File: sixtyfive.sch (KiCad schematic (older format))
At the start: 20 parts

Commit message: diagrammed mcu
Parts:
- added D? (x66): D_Small, symbol Device:D_Small
- added J?: Conn_ARM_JTAG_SWD_10, symbol Connector:Conn_ARM_JTAG_SWD_10
- added MX?: 6, symbol MX_Alps_Hybrid:MX-NoLED
- added MX?: 7, symbol MX_Alps_Hybrid:MX-NoLED
- added MX?: Y, symbol MX_Alps_Hybrid:MX-NoLED
- added MX?: U, symbol MX_Alps_Hybrid:MX-NoLED
- added MX?: 8, symbol MX_Alps_Hybrid:MX-NoLED
- added MX?: 9, symbol MX_Alps_Hybrid:MX-NoLED
- added MX?: I, symbol MX_Alps_Hybrid:MX-NoLED
- added MX?: O, symbol MX_Alps_Hybrid:MX-NoLED
- added MX?: 0, symbol MX_Alps_Hybrid:MX-NoLED
- added MX?: -, symbol MX_Alps_Hybrid:MX-NoLED
- added MX?: P, symbol MX_Alps_Hybrid:MX-NoLED
- added MX?: [{, symbol MX_Alps_Hybrid:MX-NoLED
- added MX?: =, symbol MX_Alps_Hybrid:MX-NoLED
- added MX?: Backspace, symbol MX_Alps_Hybrid:MX-NoLED
- added MX?: ]}, symbol MX_Alps_Hybrid:MX-NoLED
- added MX?: \\|, symbol MX_Alps_Hybrid:MX-NoLED
- added MX?: H, symbol MX_Alps_Hybrid:MX-NoLED
- added MX?: J, symbol MX_Alps_Hybrid:MX-NoLED
- added MX?: N, symbol MX_Alps_Hybrid:MX-NoLED
- added MX?: M, symbol MX_Alps_Hybrid:MX-NoLED
- added MX?: K, symbol MX_Alps_Hybrid:MX-NoLED
- added MX?: L, symbol MX_Alps_Hybrid:MX-NoLED
- added MX?: ,<, symbol MX_Alps_Hybrid:MX-NoLED
- added MX?: .>, symbol MX_Alps_Hybrid:MX-NoLED
- added MX?: :;, symbol MX_Alps_Hybrid:MX-NoLED
- added MX?: \"', symbol MX_Alps_Hybrid:MX-NoLED
- added MX?: ?/, symbol MX_Alps_Hybrid:MX-NoLED
- added MX?: RightShift, symbol MX_Alps_Hybrid:MX-NoLED
- added MX?: Enter, symbol MX_Alps_Hybrid:MX-NoLED
- added MX?: PgUp, symbol MX_Alps_Hybrid:MX-NoLED
- added MX?: Up, symbol MX_Alps_Hybrid:MX-NoLED
- added MX? (x2): MX-NoLED, symbol MX_Alps_Hybrid:MX-NoLED
- added MX?: 2, symbol MX_Alps_Hybrid:MX-NoLED
- added MX?: 3, symbol MX_Alps_Hybrid:MX-NoLED
- added MX?: W, symbol MX_Alps_Hybrid:MX-NoLED
- added MX?: E, symbol MX_Alps_Hybrid:MX-NoLED
- added MX?: 4, symbol MX_Alps_Hybrid:MX-NoLED
- added MX?: 5, symbol MX_Alps_Hybrid:MX-NoLED
- added MX?: R, symbol MX_Alps_Hybrid:MX-NoLED
- added MX?: T, symbol MX_Alps_Hybrid:MX-NoLED
- added MX?: S, symbol MX_Alps_Hybrid:MX-NoLED
- added MX?: D, symbol MX_Alps_Hybrid:MX-NoLED
- added MX?: X, symbol MX_Alps_Hybrid:MX-NoLED
- added MX?: C, symbol MX_Alps_Hybrid:MX-NoLED
- added MX?: F, symbol MX_Alps_Hybrid:MX-NoLED
- added MX?: G, symbol MX_Alps_Hybrid:MX-NoLED
- added MX?: V, symbol MX_Alps_Hybrid:MX-NoLED
- added MX?: B, symbol MX_Alps_Hybrid:MX-NoLED
- added MX?: ESC, symbol MX_Alps_Hybrid:MX-NoLED
- added MX?: 1, symbol MX_Alps_Hybrid:MX-NoLED
- added MX?: Tab, symbol MX_Alps_Hybrid:MX-NoLED
- added MX?: Q, symbol MX_Alps_Hybrid:MX-NoLED
- added MX?: CapsLock, symbol MX_Alps_Hybrid:MX-NoLED
- added MX?: A, symbol MX_Alps_Hybrid:MX-NoLED
- added MX?: LShift, symbol MX_Alps_Hybrid:MX-NoLED
- added MX?: Z, symbol MX_Alps_Hybrid:MX-NoLED
- added MX?: LControl, symbol MX_Alps_Hybrid:MX-NoLED
- added MX?: LOS, symbol MX_Alps_Hybrid:MX-NoLED
- added MX?: LAlt, symbol MX_Alps_Hybrid:MX-NoLED
- added MX?: Space, symbol MX_Alps_Hybrid:MX-NoLED
- added MX?: RAlt, symbol MX_Alps_Hybrid:MX-NoLED
- added MX?: RControl, symbol MX_Alps_Hybrid:MX-NoLED
- added MX?: Left, symbol MX_Alps_Hybrid:MX-NoLED
- added MX?: Down, symbol MX_Alps_Hybrid:MX-NoLED
- added MX?: Right, symbol MX_Alps_Hybrid:MX-NoLED
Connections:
- net 3.3V: now also J?.1 (VTref)
- net GND: now also J?.3 (GND), J?.5 (GND), J?.9 (GNDDetect)
- net Col4: now reaches U?.10 (PA0)
- net Col4: now also MX?.1 (COL), MX?.1 (COL), MX?.1 (COL), MX?.1 (COL)
- net Col3: now reaches U?.11 (PA1)
- net Col3: now also MX?.1 (COL), MX?.1 (COL), MX?.1 (COL), MX?.1 (COL), MX?.1 (COL)
- net Col2: now reaches U?.12 (PA2)
- net Col2: now also MX?.1 (COL), MX?.1 (COL), MX?.1 (COL), MX?.1 (COL), MX?.1 (COL)
- net Row5: now reaches U?.13 (PA3)
- net Row5: now also D?.1 (K), D?.1 (K), D?.1 (K), D?.1 (K), D?.1 (K), D?.1 (K), D?.1 (K), D?.1 (K), D?.1 (K), D?.1 (K)
- net Col14: now reaches U?.14 (PA4)
- net Col14: now also MX?.1 (COL), MX?.1 (COL), MX?.1 (COL), MX?.1 (COL), MX?.1 (COL)
- net Col13: now reaches U?.15 (PA5)
- net Col13: now also MX?.1 (COL), MX?.1 (COL), MX?.1 (COL), MX?.1 (COL), MX?.1 (COL)
- net LED_PWM: now reaches U?.16 (PA6)
- net Col12: now reaches U?.17 (PA7)
- net Col12: now also MX?.1 (COL), MX?.1 (COL), MX?.1 (COL), MX?.1 (COL), MX?.1 (COL)
- net Col9: now reaches U?.18 (PB0)
- net Col9: now also MX?.1 (COL), MX?.1 (COL), MX?.1 (COL), MX?.1 (COL), MX?.1 (COL)
- net Col10: now reaches U?.19 (PB1)
- net Col10: now also MX?.1 (COL), MX?.1 (COL), MX?.1 (COL), MX?.1 (COL), MX?.1 (COL)
- net Extra1: now reaches U?.2 (PC13)
- net Col11: now reaches U?.20 (PB2)
- net Col11: now also MX?.1 (COL), MX?.1 (COL), MX?.1 (COL), MX?.1 (COL), MX?.1 (COL)
- net Row3: now reaches U?.21 (PB10)
- net Row3: now also D?.1 (K), D?.1 (K), D?.1 (K), D?.1 (K), D?.1 (K), D?.1 (K), D?.1 (K), D?.1 (K), D?.1 (K), D?.1 (K), D?.1 (K), D?.1 (K), D?.1 (K), D?.1 (K)
- net Row4: now reaches U?.22 (PB11)
- net Row4: now also D?.1 (K), D?.1 (K), D?.1 (K), D?.1 (K), D?.1 (K), D?.1 (K), D?.1 (K), D?.1 (K), D?.1 (K), D?.1 (K), D?.1 (K), D?.1 (K), D?.1 (K), D?.1 (K)
- net Col1: now reaches U?.25 (PB12)
- net Col1: now also MX?.1 (COL), MX?.1 (COL), MX?.1 (COL), MX?.1 (COL), MX?.1 (COL)
- net Extra7: now reaches U?.26 (PB13)
- net Extra8: now reaches U?.27 (PB14)
- net RGB3V3: now reaches U?.28 (PB15)
- net Extra9: now reaches U?.29 (PA8)
- net Col7: now reaches U?.3 (PC14)
- net Col7: now also MX?.1 (COL), MX?.1 (COL), MX?.1 (COL), MX?.1 (COL), MX?.1 (COL)
- net Extra10: now reaches U?.30 (PA9)
- net Extra11: now reaches U?.31 (PA10)
- net SWDIO: now reaches U?.34 (PA13)
- net SWDIO: now also J?.2 (SWDIO/TMS)
- net SWCLK: now reaches U?.37 (PA14)
- net SWCLK: now also J?.4 (SWDCLK/TCK)
- net Extra12: now reaches U?.38 (PA15)
- net Extra2: now reaches U?.39 (PB3)
- net Col8: now reaches U?.4 (PC15)
- net Col8: now also MX?.1 (COL), MX?.1 (COL), MX?.1 (COL), MX?.1 (COL)
- net Extra3: now reaches U?.40 (PB4)
- net Extra4: now reaches U?.41 (PB5)
- net Extra5: now reaches U?.42 (PB6)
- net Row1: now reaches U?.43 (PB7)
- net Row1: now also D?.1 (K), D?.1 (K), D?.1 (K), D?.1 (K), D?.1 (K), D?.1 (K), D?.1 (K), D?.1 (K), D?.1 (K), D?.1 (K), D?.1 (K), D?.1 (K), D?.1 (K), D?.1 (K)
- net BOOT0: now reaches U?.44 (BOOT0)
- net Row2: now reaches U?.45 (PB8)
- net Row2: now also D?.1 (K), D?.1 (K), D?.1 (K), D?.1 (K), D?.1 (K), D?.1 (K), D?.1 (K), D?.1 (K), D?.1 (K), D?.1 (K), D?.1 (K), D?.1 (K), D?.1 (K), D?.1 (K)
- net Extra6: now reaches U?.46 (PB9)
- net Col5: now reaches U?.5 (PF0)
- net Col5: now also MX?.1 (COL), MX?.1 (COL), MX?.1 (COL), MX?.1 (COL)
- net Col6: now reaches U?.6 (PF1)
- net Col6: now also MX?.1 (COL), MX?.1 (COL), MX?.1 (COL), MX?.1 (COL)
- net NRST: now reaches U?.7 (NRST)
- net NRST: now also J?.10 (~RESET~)
- new net: D?.2 (A), MX?.2 (ROW) (x66)
- no-connect marks 2 -> 4

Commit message: Added rest of stuff I'm pulling in from Tsuki
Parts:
- added C?: 4.7n, symbol Device:C_Small
- added C?: 10u, symbol Device:C_Small
- added C? (x10): 100n, symbol Device:C_Small
- added C?: 4.7nF, symbol Device:C_Small
- added D?: 1N4148, symbol Device:D_Small
- added D? (x10): WS2812B, LED_SMD:LED_WS2812B_PLCC4_5.0x5.0mm_P3.2mm, symbol LED:WS2812B
- added J?: Conn_01x12, symbol Connector_Generic:Conn_01x12
- added Q?: DTC123J, symbol Transistor_BJT:DTC123J
- added Q?: BSS138, Package_TO_SOT_SMD:SOT-23, symbol Transistor_FET:BSS138
- added R?: 100k, symbol Device:R_Small
- added R? (x10): 5.1R, symbol Device:R_Small
- added R? (x2): 10k, symbol Device:R_Small
- added R?: 1M, symbol Device:R_Small
- added SW?: SW_Push, symbol Switch:SW_Push
- added U?: USBLC6-2SC6, Package_TO_SOT_SMD:SOT-23-6, symbol Power_Protection:USBLC6-2SC6
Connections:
- net 3.3V: now also Q?.1 (G), R?.1, SW?.1
- net 5V: now also R?.1, R?.1, R?.1, R?.1, R?.1, R?.1, R?.1, R?.1, R?.1, R?.1, R?.1
- net BOOT0: now also C?.1, D?.1 (K), R?.1
- net D+: now also U?.3 (I/O2)
- net D-: now also U?.1 (I/O1)
- net DBus+: now also U?.4 (I/O2)
- net DBus-: now also U?.6 (I/O1)
- net Extra1: now also J?.1 (Pin_1)
- net Extra10: now also J?.10 (Pin_10)
- net Extra11: now also J?.11 (Pin_11), J?.12 (Pin_12)
- net Extra2: now also J?.2 (Pin_2)
- net Extra3: now also J?.3 (Pin_3)
- net Extra4: now also J?.4 (Pin_4)
- net Extra5: now also J?.5 (Pin_5)
- net Extra6: now also J?.6 (Pin_6)
- net Extra7: now also J?.7 (Pin_7)
- net Extra8: now also J?.8 (Pin_8)
- net Extra9: now also J?.9 (Pin_9)
- net GND: now also C?.1, C?.1, C?.1, C?.1, C?.1, C?.1, C?.1, C?.1, C?.1, C?.1, C?.1, C?.2, C?.2, D?.3 (VSS), D?.3 (VSS), D?.3 (VSS), D?.3 (VSS), D?.3 (VSS), D?.3 (VSS), D?.3 (VSS), D?.3 (VSS), D?.3 (VSS), D?.3 (VSS), Q?.2 (E), R?.1, R?.2, U?.2 (GND)
- net NRST: now also C?.2, Q?.3 (C)
- net VBUS: now also U?.5 (VBUS)
- net at USB?.S1 (SHIELD): now also C?.1, R?.2
- new net: D?.2 (A), Q?.1 (B), SW?.2
- new net: C?.2, D?.1 (VDD), R?.2 (x10)
- new net: D?.2 (DOUT), D?.4 (DIN) (x9)
- new net RGB_3V3: Q?.2 (S), R?.2
- new net RGB_5V: D?.4 (DIN), Q?.3 (D), R?.2
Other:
- moved on the sheet: C?, D?, F?, J?, MX?, RSI1, RSO1, U?

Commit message: labeled everything? maybe?
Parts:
- added CSH1: 4.7nF, symbol Device:C_Small
- added RGND?: R01, symbol Device:R_Small
- added RSH1: 1M, symbol Device:R_Small
- CSI?, CSO?: renamed from C?; value C_Small -> 1u
- DF?: renamed from D?; value D_TVS -> SMF9.0CA
- DS?: renamed from D?; value D_Schottky -> RB060M-60TR
- F?: value Polyfuse_Small -> 1.5A trip PTC
- gave numbers to parts that had none: 13
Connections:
- net GND: now also CSH1.1, RGND?.2, RSH1.2
- net GNDD: now also RGND?.1
- new net CASE: CSH1.2, RSH1.1

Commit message: Added footprints for most things
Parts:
- CB1, CB2, CB3, CB4, CB5, CB6, CB7, CB8: renamed from CB?; footprint (none) -> Capacitor_SMD:C_0402_1005Metric
- CR1, CR2: renamed from CR?; footprint (none) -> Capacitor_SMD:C_0805_2012Metric_Pad1.15x1.40mm_HandSolder
- CRGB1, CRGB10, CRGB2, CRGB3, CRGB4, CRGB5, CRGB6, CRGB7, CRGB8, CRGB9: renamed from CRGB?; footprint (none) -> Capacitor_SMD:C_0805_2012Metric
- CSH1, CSH2: footprint (none) -> Capacitor_SMD:C_0805_2012Metric
- CSI1: renamed from CSI?; footprint (none) -> Capacitor_SMD:C_0805_2012Metric_Pad1.15x1.40mm_HandSolder
- CSO1: renamed from CSO?; footprint (none) -> Capacitor_SMD:C_0805_2012Metric_Pad1.15x1.40mm_HandSolder
- D1, D10, D11, D12, D13, D14, D15, D16, D17, D18, D19, D2, D20, D21, D22, D23, D24, D25, D26, D27, D28, D29, D3, D30, D31, D32, D33, D34, D35, D36, D37, D38, D39, D4, D40, D41, D42, D43, D44, D45, D46, D47, D48, D49, D5, D50, D51, D52, D53, D54, D55, D56, D57, D58, D59, D6, D60, D61, D62, D63, D64, D65, D66, D7, D8, D9: renamed from D?; footprint (none) -> Diode_SMD:D_SOD-123
- DF1: renamed from DF?; footprint (none) -> Diode_SMD:D_SOD-123
- DR1: renamed from DR?; footprint (none) -> Diode_SMD:D_SOD-123
- DS1: renamed from DS?; footprint (none) -> Diode_SMD:D_SOD-123
- F1: renamed from F?; footprint (none) -> Fuse:Fuse_1812_4532Metric
- J1: renamed from J?; footprint (none) -> Connector_PinHeader_2.54mm:PinHeader_1x12_P2.54mm_Vertical
- MX1, MX10, MX11, MX12, MX13, MX16, MX17, MX18, MX19, MX2, MX20, MX21, MX22, MX23, MX24, MX25, MX26, MX27, MX3, MX30, MX31, MX32, MX33, MX34, MX35, MX36, MX37, MX38, MX39, MX4, MX40, MX42, MX44, MX45, MX46, MX47, MX48, MX49, MX5, MX50, MX51, MX52, MX53, MX55, MX56, MX6, MX63, MX64, MX65, MX66, MX7, MX8, MX9: renamed from MX?; footprint (none) -> MX_Only:MXOnly-1U-Hotswap
- MX14: renamed from MX?; footprint (none) -> MX_Only:MXOnly-2U-Hotswap
- MX15, MX28: renamed from MX?; footprint (none) -> MX_Only:MXOnly-1.5U-Hotswap
- MX29, MX54: renamed from MX?; footprint (none) -> MX_Only:MXOnly-1.75U-Hotswap
- MX41, MX43: renamed from MX?; footprint (none) -> MX_Only:MXOnly-2.25U-Hotswap
- MX57, MX58, MX59, MX61, MX62: renamed from MX?; footprint (none) -> MX_Only:MXOnly-1.25U-Hotswap
- MX60: renamed from MX?; footprint (none) -> MX_Only:MXOnly-6.25U-Hotswap
- QRST1: footprint (none) -> Package_TO_SOT_SMD:SOT-23
- RCC1, RCC2, RSH1, RSH2, RSI1, RSO1: footprint (none) -> Resistor_SMD:R_1206_3216Metric
- RGND1: renamed from RGND?; footprint (none) -> Resistor_SMD:R_1206_3216Metric
- RR1: renamed from RR?; footprint (none) -> Resistor_SMD:R_1206_3216Metric
- RRGB1, RRGB10, RRGB2, RRGB3, RRGB4, RRGB5, RRGB6, RRGB7, RRGB8, RRGB9: renamed from RRGB?; footprint (none) -> Resistor_SMD:R_1206_3216Metric
- RS1, RS2: renamed from RS?; footprint (none) -> Resistor_SMD:R_1206_3216Metric
- USB1: renamed from USB?; footprint (none) -> Connector_USB:USB_C_Receptacle_GCT_USB4085
- gave numbers to parts that had none: 16

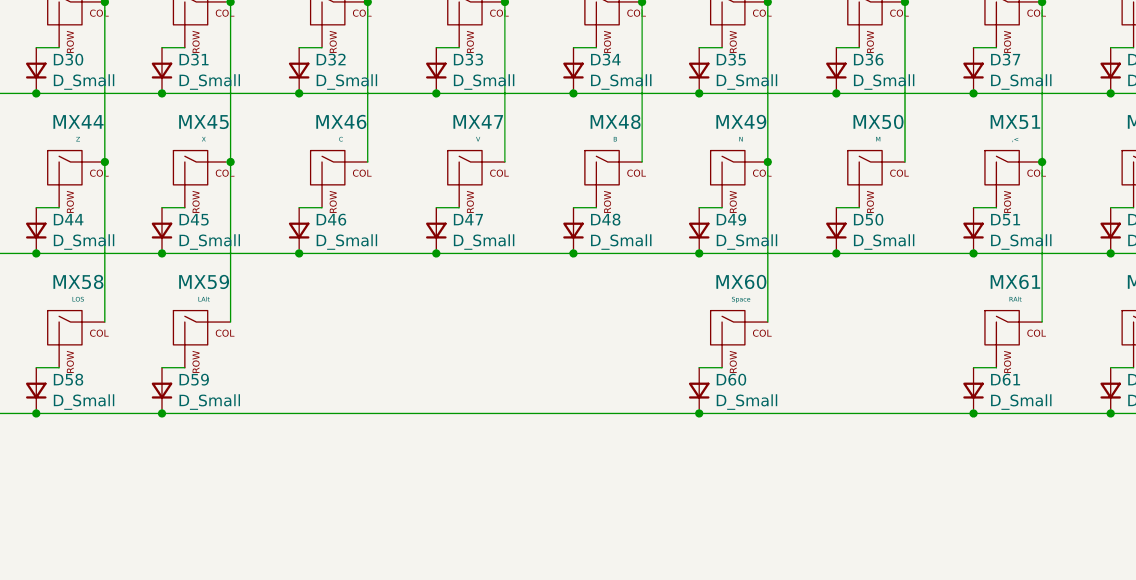
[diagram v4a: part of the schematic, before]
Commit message: Placed all the switches, all the diodes!
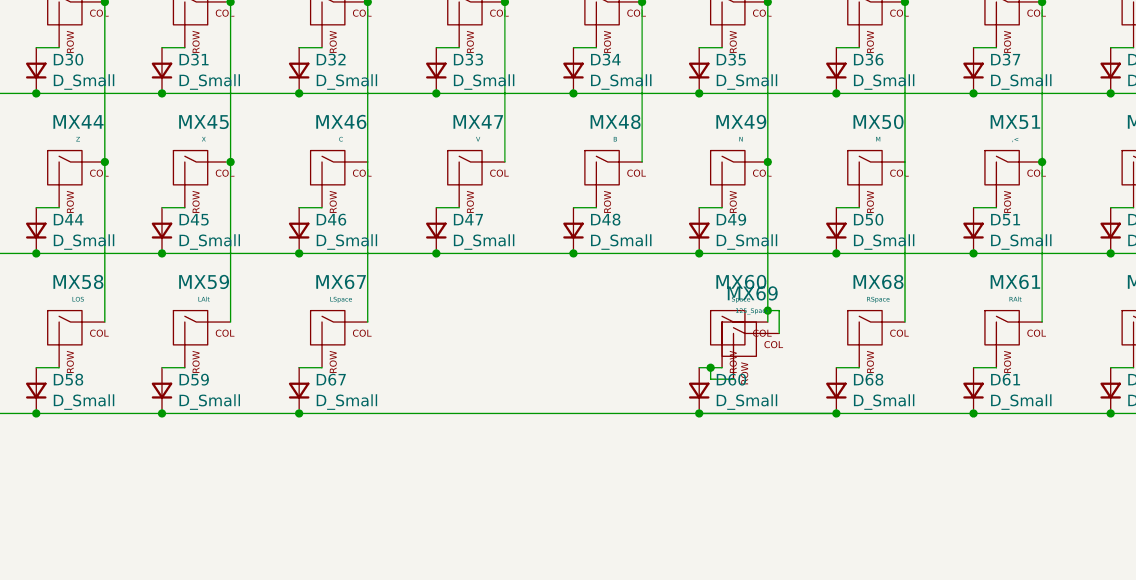
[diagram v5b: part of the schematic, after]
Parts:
- added D67, D68: D_Small, Diode_SMD:D_SOD-123, symbol Device:D_Small
- added MX67: LSpace, MX_Only:MXOnly-2.75U-Hotswap-ReversedStabilizers, symbol MX_Alps_Hybrid:MX-NoLED
- added MX68: RSpace, MX_Only:MXOnly-2.25U-Hotswap-ReversedStabilizers, symbol MX_Alps_Hybrid:MX-NoLED
- added MX69: 125_Space, MX_Only:MXOnly-1.25U-Hotswap, symbol MX_Alps_Hybrid:MX-NoLED
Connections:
- net Col4: now also MX67.1 (COL)
- net Col7: now also MX69.1 (COL)
- net Col8: now also MX68.1 (COL)
- net Row5: now also D67.1 (K), D68.1 (K)
- net at D60.2 (A), MX60.2 (ROW): now also MX69.2 (ROW)
- new net: D67.2 (A), MX67.2 (ROW)
- new net: D68.2 (A), MX68.2 (ROW)
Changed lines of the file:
@@
 $EndComp
 Wire Wire Line
-	24650 13700 24750 13700
+	24650 13700 24700 13700
 $Comp
 L MX_Alps_Hybrid:MX-NoLED MX61
@@
 Connection ~ 24650 13900
 Wire Wire Line
-	24650 13900 22300 13900
+	24650 13900 22900 13900
 Connection ~ 25850 13900
 Wire Wire Line
-	25850 13900 24650 13900
+	25850 13900 25250 13900
 Connection ~ 26450 13900
 Wire Wire Line
@@
 	24400 12100 24400 11400
 Wire Wire Line
-	24950 13500 24950 12800
+	24950 13500 24950 13450
 Connection ~ 24950 10700
 Wire Wire Line
@@
 	25100 19600 25100 19550
 Connection ~ 25100 19550
+$Comp
+L MX_Alps_Hybrid:MX-NoLED MX67
+U 1 1 613EC2DC
+P 23050 13550
+F 0 "MX67" H 23083 13773 60  0000 C CNN
+F 1 "LSpace" H 23083 13699 20  0000 C CNN
+F 2 "MX_Only:MXOnly-2.75U-Hotswap-ReversedStabilizers" H 22425 13525 60  0001 C CNN
+F 3 "" H 22425 13525 60  0001 C CNN
+	1    23050 13550
+	1    0    0    -1
+$EndComp
+$Comp
+L Device:D_Small D67
+U 1 1 613EC2E2
+P 22900 13800
+F 0 "D67" V 22946 13730 50  0000 R CNN
+F 1 "D_Small" V 22855 13730 50  0000 R CNN
+F 2 "Diode_SMD:D_SOD-123" V 22900 13800 50  0001 C CNN
+F 3 "~" V 22900 13800 50  0001 C CNN
+	1    22900 13800
+	0    -1   -1   0
+$EndComp
+Wire Wire Line
+	22900 13700 23000 13700
+Wire Wire Line
+	23200 13500 23200 12800
+$Comp
+L MX_Alps_Hybrid:MX-NoLED MX68
+U 1 1 61434797
+P 25400 13550
+F 0 "MX68" H 25433 13773 60  0000 C CNN
+F 1 "RSpace" H 25433 13699 20  0000 C CNN
+F 2 "MX_Only:MXOnly-2.25U-Hotswap-ReversedStabilizers" H 24775 13525 60  0001 C CNN
+F 3 "" H 24775 13525 60  0001 C CNN
+	1    25400 13550
+	1    0    0    -1
+$EndComp
+$Comp
+L Device:D_Small D68
+U 1 1 6143479D
+P 25250 13800
+F 0 "D68" V 25296 13730 50  0000 R CNN
+F 1 "D_Small" V 25205 13730 50  0000 R CNN
+F 2 "Diode_SMD:D_SOD-123" V 25250 13800 50  0001 C CNN
+F 3 "~" V 25250 13800 50  0001 C CNN
+	1    25250 13800
+	0    -1   -1   0
+$EndComp
+Wire Wire Line
+	25250 13700 25350 13700
+Wire Wire Line
+	25550 13500 25550 12800
+$Comp
+L MX_Alps_Hybrid:MX-NoLED MX69
+U 1 1 6147E109
+P 24850 13600
+F 0 "MX69" H 24883 13823 60  0000 C CNN
+F 1 "125_Space" H 24883 13749 20  0000 C CNN
+F 2 "MX_Only:MXOnly-1.25U-Hotswap" H 24225 13575 60  0001 C CNN
+F 3 "" H 24225 13575 60  0001 C CNN
+	1    24850 13600
+	1    0    0    -1
+$EndComp
+Wire Wire Line
+	24700 13750 24800 13750
+Wire Wire Line
+	25000 13550 25000 13450
+Wire Wire Line
+	25000 13450 24950 13450
+Connection ~ 24950 13450
+Wire Wire Line
+	24950 13450 24950 12800
+Wire Wire Line
+	24700 13750 24700 13700
+Connection ~ 24700 13700
+Wire Wire Line
+	24700 13700 24750 13700
+Wire Wire Line
+	22300 13900 22900 13900
+Connection ~ 22900 13900
+Wire Wire Line
+	24650 13900 25250 13900
+Connection ~ 25250 13900
+Wire Wire Line
+	25250 13900 24650 13900
 $EndSCHEMATC
